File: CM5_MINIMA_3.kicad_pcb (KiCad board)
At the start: 6 copper layers, 61.2 x 64.2 mm, 112 parts, among them CN1 SM02B-SRSS-TB (LF)(SN), J101 TYPEC-305-ACP16H458, J501 GT-HD001B-CNNG1, J502 I2C, J503 SPI, J601 JST_SHBM04B-SRSS-TB, J701 Bus_M.2_Socket_M, J802 Conn_01x22_Female, M701 M.2 Solder Nut, M702 M.2 Solder Nut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

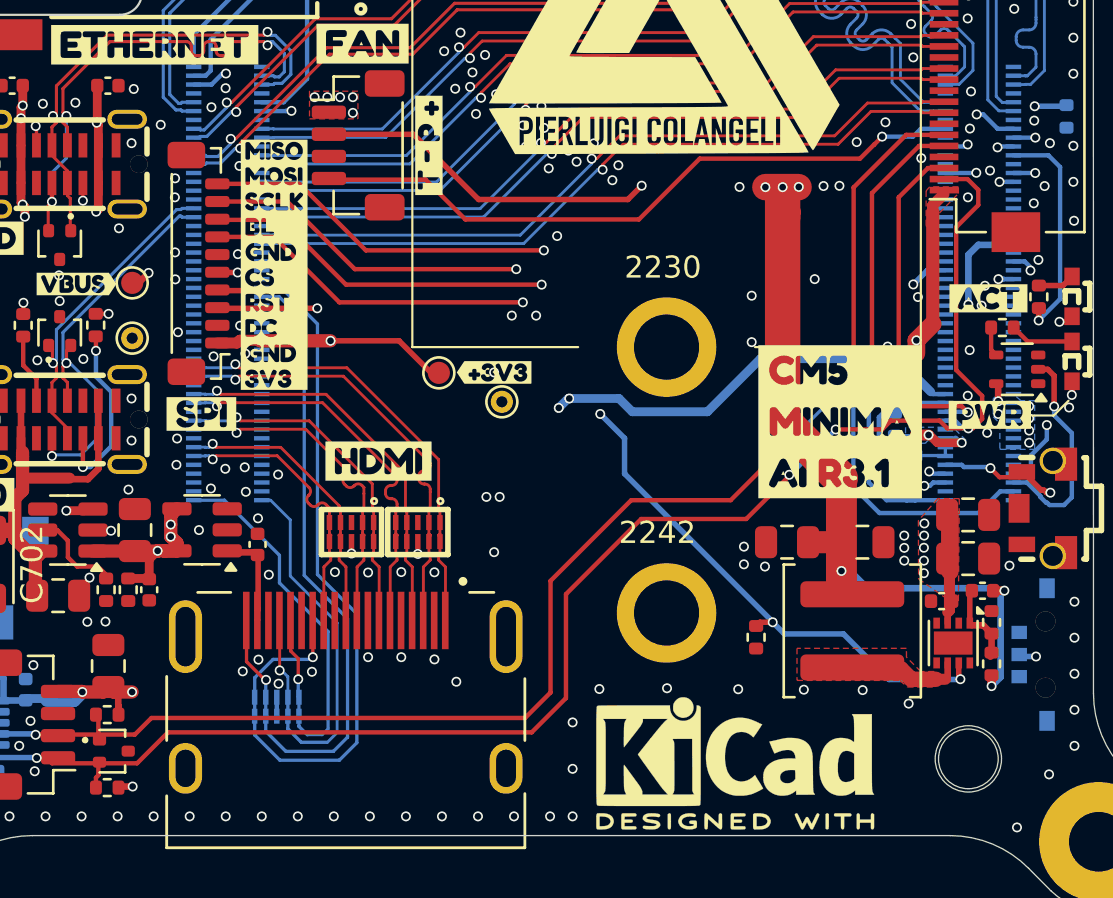
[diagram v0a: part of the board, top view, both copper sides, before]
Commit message: swapped I2C bus from 0 to 1
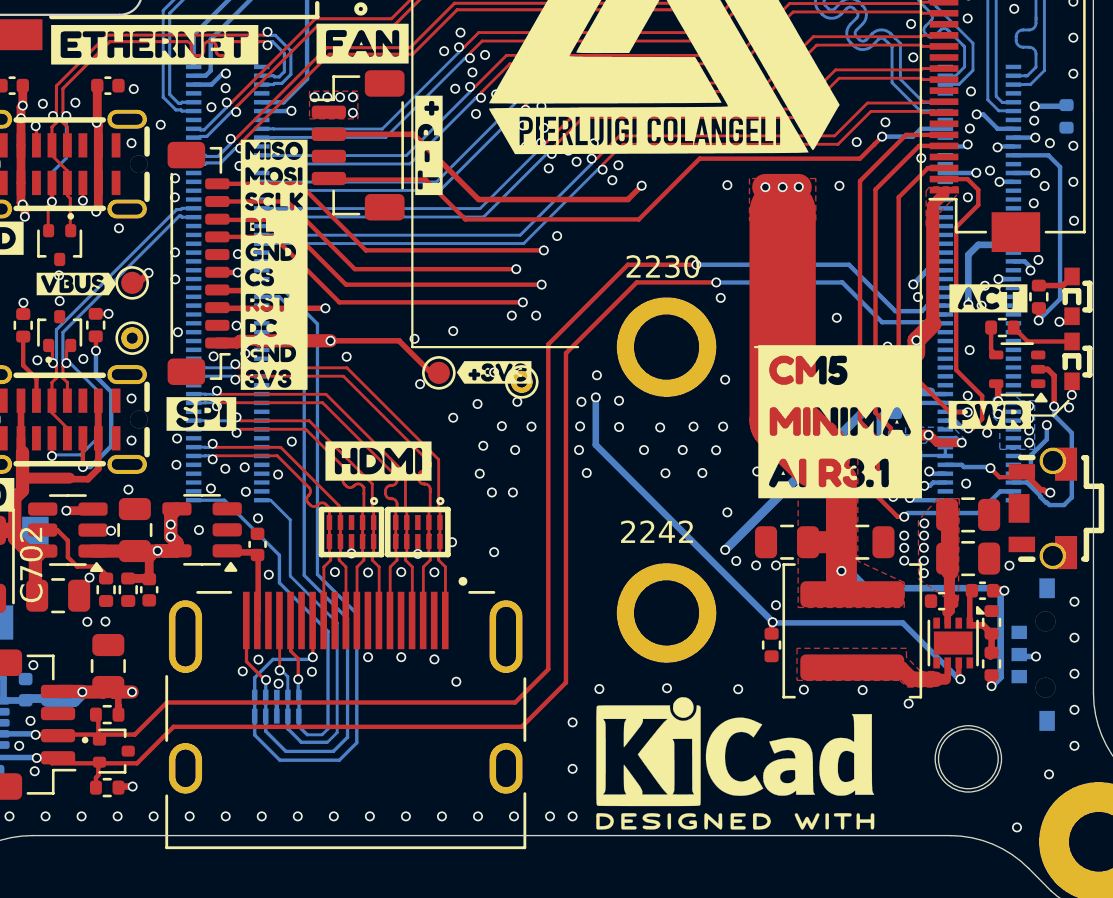
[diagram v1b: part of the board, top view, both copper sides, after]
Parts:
- moved TP106 1.27 mm to (107.0, 60.5)
- moved R704 0.78 mm to (118.3, 72.5)
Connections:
- D502 pad 1: /SCL -> /IO/SCL
- D502 pad 2: /SDA -> /IO/SDA
- J502 pad 1: /SDA -> /IO/SDA
- J502 pad 2: /SCL -> /IO/SCL
- J802 pad 20: /SCL -> /CM5/SCL0
- J802 pad 21: /SDA -> /CM5/SDA0
- Module301 pad 56: /CM5/GPIO3 -> /IO/SCL
- Module301 pad 58: /CM5/GPIO2 -> /IO/SDA
- Module301 pad 80: /SCL -> /CM5/SCL0
- Module301 pad 82: /SDA -> /CM5/SDA0
- R501 pad 2: /SDA -> /IO/SDA
- R502 pad 2: /SCL -> /IO/SCL
- U1 pad 4: /SCL -> /IO/SCL
- U1 pad 6: /SDA -> /IO/SDA
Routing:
- net /SDA: track 70.9 -> 0.00 mm, vias 4 -> 0
- net /SCL: track 67.7 -> 0.00 mm, vias 4 -> 0
- net /IO/SDA: track 0.00 -> 64.2 mm, vias 0 -> 2
- net /IO/SCL: track 0.00 -> 62.6 mm, vias 0 -> 2
- net /CM5/SCL0: track 0.00 -> 15.2 mm, vias 0 -> 1
- net /CM5/SDA0: track 0.00 -> 15.0 mm, vias 0 -> 1
- net +BATT: track 69.0 -> 61.4 mm, vias 4 -> 3
- net /CM5/CAM_GPIO1: track 21.1 -> 20.2 mm
- net /CM5/PCIE_PI.PWR_EN: track 49.7 -> 49.1 mm
- net /CM5/CS_GPIO18: track 42.2 -> 41.7 mm
- net /CM5/RST_GPIO27: track 39.4 -> 38.9 mm
- net GND: vias 256 -> 290

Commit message: drc ok
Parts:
- moved TP103 2.10 mm to (101.3, 59.4)
- moved kibuzzard-6773B9CA 1.92 mm to (104.0, 59.4)
- moved TP106 0.57 mm to (106.6, 60.9)
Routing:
- net +BATT: track 61.4 -> 58.5 mm
- net +3V3_PI: track 142.6 -> 140.3 mm
- net /CM5/PCIE_PI.PWR_EN: track 49.1 -> 47.9 mm
- net GND: vias 290 -> 288
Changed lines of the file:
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@@
 	(footprint "TestPoint:TestPoint_Pad_D1.0mm"
 		(layer "F.Cu")
-		(at 103.3 60.14)
+		(at 101.34 59.39)
 		(descr "SMD pad as test Point, diameter 1.0mm")
 		(tags "test point SMD pad")
@@
 	(footprint "kibuzzard-6773B9CA"
 		(layer "F.Cu")
-		(at 105.8 60.12)
+		(at 104 59.44)
 		(descr "Generated with KiBuzzard")
 		(tags "kb_params=eyJBbGlnbm1lbnRDaG9pY2UiOiAiQ2VudGVyIiwgIkNhcExlZnRDaG9pY2UiOiAiPCIsICJDYXBSaWdodENob2ljZSI6ICJdIiwgIkZvbnRDb21ib0JveCI6ICJGcmVkZHlTcGFyay1SZWd1bGFyIiwgIkhlaWdodEN0cmwiOiAwLjgsICJMYXllckNvbWJvQm94IjogIkYuU2lsa1MiLCAiTGluZVNwYWNpbmdDdHJsIjogMS4wLCAiTXVsdGlMaW5lVGV4dCI6ICIrM1YzIiwgIlBhZGRpbmdCb3R0b21DdHJsIjogMS4wLCAiUGFkZGluZ0xlZnRDdHJsIjogMi4wLCAiUGFkZGluZ1JpZ2h0Q3RybCI6IDIuMCwgIlBhZGRpbmdUb3BDdHJsIjogMS4wLCAiV2lkdGhDdHJsIjogMC4wLCAiYWR2YW5jZWRDaGVja2JveCI6IGZhbHNlLCAiaW5saW5lRm9ybWF0VGV4dGJveCI6IGZhbHNlLCAibGluZW92ZXJTdHlsZUNob2ljZSI6ICJTcXVhcmUiLCAibGluZW92ZXJUaGlja25lc3NDdHJsIjogMX0=")
@@
 	(footprint "TestPoint:TestPoint_THTPad_D1.0mm_Drill0.5mm"
 		(layer "F.Cu")
-		(at 107.05 60.55)
+		(at 106.56 60.85)
 		(descr "THT pad as test Point, diameter 1.0mm, hole diameter 0.5mm")
 		(tags "test point THT pad")
@@
 	)
 	(via
-		(at 109.69 62.56)
-		(size 0.45)
-		(drill 0.3)
-		(layers "F.Cu" "B.Cu")
-		(free yes)
-		(net 1)
-	)
-	(via
 		(at 118.24 31.7)
 		(size 0.45)
@@
 	)
 	(via
-		(at 117.65 68.85)
+		(at 117.84 68.88)
 		(size 0.45)
 		(drill 0.3)
@@
 	)
 	(via
-		(at 118.55 68.85)
+		(at 118.46 68.87)
 		(size 0.45)
 		(drill 0.3)
@@
 	)
 	(via
-		(at 106.85 61.45)
-		(size 0.45)
-		(drill 0.3)
-		(layers "F.Cu" "B.Cu")
-		(free yes)
-		(net 1)
-	)
-	(via
 		(at 108.435 41.28)
 		(size 0.45)
@@
 	)
 	(via
-		(at 116.75 68.65)
+		(at 118.16 69.42)
 		(size 0.45)
 		(drill 0.3)
@@
 	)
 	(via
-		(at 109.75 61.45)
+		(at 110.57 59.11)
 		(size 0.45)
 		(drill 0.3)
@@
 	)
 	(segment
-		(start 102.95 60.14)
-		(end 103.3 60.14)
-		(width 0.25)
-		(layer "F.Cu")
-		(net 54)
-	)
-	(segment
 		(start 88.8 75.2)
 		(end 88.81 75.21)
@@
 	)
 	(segment
-		(start 101.5 58.69)
-		(end 102.95 60.14)
-		(width 0.25)
-		(layer "F.Cu")
-		(net 54)
-	)
-	(segment
 		(start 88.81 75.21)
 		(end 88.81 75.6)
@@
 	)
 	(segment
-		(start 98.4 58.69)
-		(end 101.5 58.69)
-		(width 0.25)
-		(layer "F.Cu")
-		(net 54)
-	)
-	(segment
 		(start 88.35 74.35)
 		(end 88.8 74.8)
@@
 	)
 	(segment
+		(start 100.64 58.69)
+		(end 101.34 59.39)
+		(width 0.25)
+		(layer "F.Cu")
+		(net 54)
+	)
+	(segment
 		(start 125.64 52.85)
 		(end 125.64 57.93)
@@
 	)
 	(segment
+		(start 98.4 58.69)
+		(end 100.64 58.69)
+		(width 0.25)
+		(layer "F.Cu")
+		(net 54)
+	)
+	(segment
 		(start 88.8 74.8)
 		(end 88.8 75.2)
@@
 	)
 	(segment
+		(start 89.425 74.575)
+		(end 89.425 78.825)
+		(width 0.3)
+		(layer "B.Cu")
+		(net 54)
+	)
+	(segment
 		(start 126.672 63.1)
 		(end 126.21 63.1)
@@
 	)
 	(segment
-		(start 89.425 74.575)
-		(end 89.425 78.825)
-		(width 0.3)
-		(layer "In3.Cu")
-		(net 54)
-	)
-	(segment
 		(start 100.2 60.9)
 		(end 104.65 65.35)
@@
 	)
 	(via
-		(at 110.4 61.25)
+		(at 105.03 57.99)
 		(size 0.45)
 		(drill 0.3)
@@
 	)
 	(segment
-		(start 110.4 63.4)
-		(end 118.4 71.4)
-		(width 0.3)
-		(layer "B.Cu")
-		(net 149)
-	)
-	(segment
 		(start 93.017537 47.1)
 		(end 92.21 47.1)
@@
 	)
 	(segment
-		(start 118.43 71.45)
-		(end 124.28198 71.45)
-		(width 0.25)
+		(start 105.115 58.075)
+		(end 105.115 58.115)
+		(width 0.3)
 		(layer "B.Cu")
 		(net 149)
 	)
 	(segment
-		(start 110.4 61.25)
-		(end 110.4 63.4)
+		(start 105.115 58.115)
+		(end 118.4 71.4)
 		(width 0.3)
 		(layer "B.Cu")
@@
 	)
 	(segment
+		(start 118.43 71.45)
+		(end 124.28198 71.45)
+		(width 0.25)
+		(layer "B.Cu")
+		(net 149)
+	)
+	(segment
 		(start 93.517537 46.6)
 		(end 93.017537 47.1)
@@
 	)
 	(segment
-		(start 118.4 71.4)
-		(end 118.4 71.42)
+		(start 105.03 57.99)
+		(end 105.115 58.075)
 		(width 0.3)
 		(layer "B.Cu")
@@
 	)
 	(segment
-		(start 94.229281 47.054693)
-		(end 94.229281 47.025413)
+		(start 118.4 71.4)
+		(end 118.4 71.42)
 		(width 0.3)
-		(layer "In2.Cu")
+		(layer "B.Cu")
 		(net 149)
 	)
@@
 	)
 	(segment
-		(start 110.4 61.25)
-		(end 110.35 61.25)
-		(width 0.3)
-		(layer "In2.Cu")
-		(net 149)
-	)
-	(segment
-		(start 106.65 59.5)
-		(end 98.61 51.46)
+		(start 93.891869 46.688001)
+		(end 93.862589 46.688001)
 		(width 0.3)
 		(layer "In2.Cu")
@@
 	)
 	(segment
-		(start 93.862589 46.688001)
-		(end 93.848588 46.674)
+		(start 93.744 46.674)
+		(end 93.67 46.6)
 		(width 0.3)
 		(layer "In2.Cu")
@@
 	)
 	(segment
-		(start 110.35 61.25)
-		(end 108.6 59.5)
+		(start 98.61 51.46)
+		(end 98.61 51.435412)
 		(width 0.3)
 		(layer "In2.Cu")
@@
 	)
 	(segment
-		(start 93.891869 46.688001)
-		(end 93.862589 46.688001)
+		(start 93.862589 46.688001)
+		(end 93.848588 46.674)
 		(width 0.3)
 		(layer "In2.Cu")
@@
 	)
 	(segment
-		(start 98.61 51.435412)
-		(end 94.229281 47.054693)
+		(start 105.03 57.99)
+		(end 105.03 57.88)
 		(width 0.3)
 		(layer "In2.Cu")
@@
 	)
 	(segment
-		(start 108.6 59.5)
-		(end 106.65 59.5)
+		(start 98.61 51.435412)
+		(end 94.229281 47.054693)
 		(width 0.3)
 		(layer "In2.Cu")
@@
 	)
 	(segment
-		(start 98.61 51.46)
-		(end 98.61 51.435412)
+		(start 94.229281 47.054693)
+		(end 94.229281 47.025413)
 		(width 0.3)
 		(layer "In2.Cu")
@@
 	)
 	(segment
-		(start 93.744 46.674)
-		(end 93.67 46.6)
+		(start 105.03 57.88)
+		(end 98.61 51.46)
 		(width 0.3)
 		(layer "In2.Cu")
@@
 	)
 	(via
-		(at 116.25 68.15)
+		(at 116.6 68.24)
 		(size 0.45)
 		(drill 0.3)
@@
 	)
 	(segment
+		(start 123.4 61)
+		(end 125.55 61)
+		(width 0.4)
+		(layer "B.Cu")
+		(net 220)
+	)
+	(segment
 		(start 82.75 71.43)
-		(end 82.75 71.8)
+		(end 82.75 72.17)
+		(width 0.4)
+		(layer "B.Cu")
+		(net 220)
+	)
+	(segment
+		(start 82.42 72.5)
+		(end 82.05 72.5)
 		(width 0.4)
 		(layer "B.Cu")
@@
 	)
 	(segment
-		(start 82.75 71.8)
-		(end 82.05 72.5)
+		(start 122.29 63.34)
+		(end 122.29 62.11)
 		(width 0.4)
 		(layer "B.Cu")
@@
 	)
 	(segment
-		(start 123.4 61)
-		(end 125.55 61)
+		(start 82.75 72.17)
+		(end 82.42 72.5)
+		(width 0.4)
+		(layer "B.Cu")
+		(net 220)
+	)
+	(segment
+		(start 116.6 68.24)
+		(end 117.39 68.24)
 		(width 0.4)
 		(layer "B.Cu")
@@
 	)
 	(segment
-		(start 116.25 68.15)
+		(start 122.29 62.11)
 		(end 123.4 61)
 		(width 0.4)
@@
 	)
 	(segment
-		(start 116.25 68.15)
-		(end 111.05 68.15)
-		(width 0.4)
-		(layer "In3.Cu")
-		(net 220)
-	)
-	(segment
-		(start 111.05 68.15)
-		(end 108.6 70.6)
+		(start 117.39 68.24)
+		(end 122.29 63.34)
 		(width 0.4)
-		(layer "In3.Cu")
+		(layer "B.Cu")
 		(net 220)
 	)
 	(segment
-		(start 87.75 79.6)
-		(end 86.2 78.05)
+		(start 85.15 72.5)
+		(end 82.05 72.5)
 		(width 0.4)
 		(layer "In3.Cu")
@@
 	)
 	(segment
-		(start 86.2 78.05)
-		(end 86.2 73.55)
+		(start 116.6 72.3)
+		(end 115.16 73.74)
 		(width 0.4)
 		(layer "In3.Cu")
@@
 	)
 	(segment
-		(start 108.6 70.6)
-		(end 108.6 74)
+		(start 115.16 73.74)
+		(end 107.89 73.74)
 		(width 0.4)
 		(layer "In3.Cu")
@@
 	)
 	(segment
-		(start 81.45 72.5)
-		(end 82.05 72.5)
+		(start 86.2 75.32)
+		(end 86.2 73.55)
 		(width 0.4)
 		(layer "In3.Cu")
@@
 	)
 	(segment
-		(start 100.9 79.6)
-		(end 87.75 79.6)
+		(start 86.2 73.55)
+		(end 85.15 72.5)
 		(width 0.4)
 		(layer "In3.Cu")
@@
 	)
 	(segment
-		(start 107.05 75.55)
-		(end 104.95 75.55)
+		(start 81.45 72.5)
+		(end 82.05 72.5)
 		(width 0.4)
 		(layer "In3.Cu")
@@
 	)
 	(segment
-		(start 86.2 73.55)
-		(end 85.15 72.5)
+		(start 107.89 73.74)
+		(end 105.29 76.34)
 		(width 0.4)
 		(layer "In3.Cu")
@@
 	)
 	(segment
-		(start 85.15 72.5)
-		(end 82.05 72.5)
+		(start 105.29 76.34)
+		(end 87.22 76.34)
 		(width 0.4)
 		(layer "In3.Cu")
@@
 	)
 	(segment
-		(start 108.6 74)
-		(end 107.05 75.55)
+		(start 116.6 68.24)
+		(end 116.6 72.3)
 		(width 0.4)
 		(layer "In3.Cu")
@@
 	)
 	(segment
-		(start 104.95 75.55)
-		(end 100.9 79.6)
+		(start 87.22 76.34)
+		(end 86.2 75.32)
 		(width 0.4)
 		(layer "In3.Cu")

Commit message: eth PCB new
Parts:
- removed T401: 7498111120AR, Connector_Wuerth:7498111120AR
- added J1: GLPLX-SMT-188S7, Samacsys:GLPLXSMT188S7QQYG, F.Cu at (88.9, 36.1)
- R403, U401, U402: moved to B.Cu
- moved C401 7.55 mm to (101.2, 40.6)
- moved C101 7.20 mm to (84.0, 54.4)
- moved C102 7.05 mm to (88.3, 54.2)
- moved kibuzzard-675EDCB9 6.78 mm to (81.7, 47.3)
- moved C711 6.12 mm to (105.8, 35.0), turned to 0 degrees
- moved U401 4.11 mm to (97.5, 38.2), turned to 0 degrees
- moved U402 4.00 mm to (97.5, 34.1), turned to 0 degrees
- moved R403 3.24 mm to (87.4, 27.1)
- moved R402 1.35 mm to (101.2, 30.5), turned to 180 degrees
- moved R401 0.97 mm to (101.2, 42.3)
- moved M702 0.15 mm to (113.6, 70.8)
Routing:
- net +3V3_PI: track 140.3 -> 145.3 mm
- net Net-(J1-MP1): track 39.2 -> 35.5 mm
- net /CM5/ETH_PI.TRD3_N: track 42.8 -> 46.4 mm
- net /CM5/ETH_PI.TRD2_P: track 42.9 -> 46.5 mm
- net /CM5/ETH_PI.TRD1_N: track 42.6 -> 46.1 mm
- net /CM5/ETH_PI.TRD3_P: track 42.8 -> 46.3 mm
- net /CM5/ETH_PI.TRD1_P: track 42.5 -> 45.9 mm
- net /CM5/ETH_PI.TRD2_N: track 42.9 -> 46.2 mm
- net /CM5/nLED_SPEED_100_1000: track 57.6 -> 60.5 mm
- net /CM5/ETH_PI.TRD0_P: track 42.5 -> 45.4 mm
- net /CM5/ETH_PI.TRD0_N: track 42.5 -> 45.2 mm
- net /CM5/PCIE_PI.nCLKREQ: track 39.2 -> 40.4 mm, vias 1 -> 2
- net Net-(J1-K_GREEN): track 4.06 -> 3.06 mm
- net Net-(J1-VCC): track 3.42 -> 2.61 mm
- net /CM5/ETH_nLED_ACTIVITY: track 30.5 -> 31.3 mm
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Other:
- outline, holes or cut-outs redrawn
- board text added: "0"
- board text added: "0 mm"
- board text added: "0.0000 mm / 0.0000 mm"
- board text added: "0.01 mm"
- board text added: "0.0152 mm"
- board text added: "0.02"
- board text added: "0.035 mm"
- board text added: "0.0994 mm"
- board text added: "0.13 mm"
- board text added: "0.3000 mm"
- board text added: "0.5 mm"
- board text added: "0.55 mm"
- board text added: "1"
- board text added: "1.5296 mm"
- board text added: "2116 RC58%"
- board text added: "3.3"
- board text added: "4.45"
- board text added: "4.6"
- board text added: "6"
- board text added: "61.2046 mm x 64.2037 mm"
- board text added: "B.Cu"
- board text added: "B.Mask"
- board text added: "B.Paste"
- board text added: "B.Silkscreen"
- board text added: "BOARD CHARACTERISTICS"
- board text added: "Board Thickness:"
- board text added: "Board overall dimensions:"
- board text added: "Bottom Silk Screen"
- board text added: "Bottom Solder Mask"
- board text added: "Bottom Solder Paste"
- board text added: "Castellated pads:"
- board text added: "Color"
- board text added: "Copper Finish:"
- board text added: "Copper Layer Count:"
- board text added: "Dielectric"
- board text added: "ENIG"
- board text added: "Edge card connectors:"
- board text added: "Epsilon R"
- board text added: "F.Cu"
- board text added: "F.Mask"
- board text added: "F.Paste"
- board text added: "F.Silkscreen"
- board text added: "FR4"
- board text added: "FR4 natural"
- board text added: "Impedance Control:"
- board text added: "In1.Cu"
- board text added: "In2.Cu"
- board text added: "In3.Cu"
- board text added: "In4.Cu"
- board text added: "Layer Name"
- board text added: "Loss Tangent"
- board text added: "Material"
- board text added: "Min hole diameter:"
- board text added: "Min track/spacing:"
- board text added: "No"
- board text added: "Not specified"
- board text added: "Plated Board Edge:"
- board text added: "Thickness (mm)"
- board text added: "Top Silk Screen"
- board text added: "Top Solder Mask"
- board text added: "Top Solder Paste"
- board text added: "Type"
- board text added: "Yes"
- board text added: "copper"
- board text added: "core"
- board text added: "prepreg"
